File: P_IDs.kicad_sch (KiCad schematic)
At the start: 1 part

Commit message: bored
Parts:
- added U11: ~, symbol PID_symbols:stop
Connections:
- net 1-2: now also U11.
- net TI-HP: now also U11.
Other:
- note added: "[Normally stops are added at the Tee (circle) section]"
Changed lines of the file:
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@@
 	(rectangle
 		(start 62.23 86.36)
-		(end 186.69 121.92)
+		(end 187.325 122.555)
 		(stroke
 			(width 0)
@@
 	)
 	(rectangle
-		(start 154.94 87.63)
+		(start 154.94 88.265)
 		(end 185.42 120.904)
 		(stroke
@@
 	)
 	(rectangle
-		(start 119.38 87.63)
+		(start 119.38 88.265)
 		(end 152.4 120.904)
 		(stroke
@@
 	(text "<-Pipe label\n"
 		(exclude_from_sim no)
-		(at 164.592 99.314 0)
+		(at 164.592 98.679 0)
 		(effects
 			(font
@@
 	(text "stop\nsymbol"
 		(exclude_from_sim no)
-		(at 158.496 111.506 0)
+		(at 161.925 106.68 0)
 		(effects
 			(font
@@
 	(text "<-Pipe label\n"
 		(exclude_from_sim no)
-		(at 178.816 110.744 0)
+		(at 174.625 104.14 0)
 		(effects
 			(font
@@
 	(text "Torch Igniter Pneumatics Line"
 		(exclude_from_sim no)
-		(at 100.33 113.03 0)
+		(at 99.695 113.03 0)
 		(effects
 			(font
@@
 		)
 	)
+	(text "[Normally stops \nare added\nat the Tee \n(circle) section]"
+		(exclude_from_sim no)
+		(at 164.465 114.935 0)
+		(effects
+			(font
+				(size 1.27 1.27)
+				(color 204 102 0 1)
+			)
+		)
+	)
 	(text "->"
 		(exclude_from_sim no)
-		(at 158.75 108.712 90)
+		(at 163.83 103.505 90)
 		(effects
 			(font
@@
 	)
 	(junction
-		(at 157.734 106.68)
+		(at 157.48 101.6)
 		(diameter 0)
 		(color 0 0 0 0)
 	)
-	(wire
-		(pts
-			(xy 159.004 106.68) (xy 171.45 106.68)
-		)
-		(stroke
-			(width 0)
-			(type default)
-		)
+	(junction
+		(at 175.26 114.935)
+		(diameter 0)
+		(color 0 0 0 0)
 	)
 	(wire
@@
 	(wire
 		(pts
-			(xy 157.734 95.25) (xy 157.734 106.68)
+			(xy 175.26 111.125) (xy 175.26 114.935)
+		)
+		(stroke
+			(width 0)
+			(type default)
+		)
+	)
+	(wire
+		(pts
+			(xy 175.26 114.935) (xy 175.26 118.745)
+		)
+		(stroke
+			(width 0)
+			(type default)
+		)
+	)
+	(wire
+		(pts
+			(xy 157.48 94.615) (xy 157.48 101.6)
+		)
+		(stroke
+			(width 0)
+			(type default)
+		)
+	)
+	(wire
+		(pts
+			(xy 157.48 101.6) (xy 163.195 101.6)
 		)
 		(stroke
@@
 	(wire
 		(pts
+			(xy 157.48 101.6) (xy 157.48 106.045)
+		)
+		(stroke
+			(width 0)
+			(type default)
+		)
+	)
+	(wire
+		(pts
 			(xy 66.04 109.22) (xy 74.93 109.22)
 		)
@@
 	(wire
 		(pts
+			(xy 179.705 114.935) (xy 179.705 118.745)
+		)
+		(stroke
+			(width 0)
+			(type default)
+		)
+	)
+	(wire
+		(pts
 			(xy 66.04 93.98) (xy 74.93 93.98)
 		)
@@
 	(wire
 		(pts
-			(xy 157.734 106.68) (xy 157.734 118.11)
+			(xy 164.465 101.6) (xy 168.91 101.6)
 		)
 		(stroke
@@
 	(wire
 		(pts
-			(xy 171.45 106.68) (xy 171.45 111.76)
+			(xy 168.91 101.6) (xy 168.91 106.045)
+		)
+		(stroke
+			(width 0)
+			(type default)
+		)
+	)
+	(wire
+		(pts
+			(xy 176.53 114.935) (xy 179.705 114.935)
 		)
 		(stroke
@@
 		)
 	)
+	(global_label "TI-HP"
+		(shape input)
+		(at 179.705 114.935 270)
+		(fields_autoplaced yes)
+		(effects
+			(font
+				(size 0.254 0.254)
+			)
+			(justify right)
+		)
+		(property "Intersheetrefs" "${INTERSHEET_REFS}"
+			(at 179.705 116.6817 90)
+			(effects
+				(font
+					(size 1.27 1.27)
+				)
+				(justify right)
+				(hide yes)
+			)
+		)
+	)
 	(global_label "3-8"
 		(shape input)
@@
 	(global_label "1-2"
 		(shape input)
-		(at 157.734 99.06 0)
+		(at 157.48 98.425 0)
 		(fields_autoplaced yes)
 		(effects
@@
 		)
 		(property "Intersheetrefs" "${INTERSHEET_REFS}"
-			(at 159.1299 99.06 0)
-			(effects
-				(font
-					(size 1.27 1.27)
-				)
-				(justify left)
+			(at 158.8759 98.425 0)
+			(effects
+				(font
+					(size 1.27 1.27)
+				)
+				(justify left)
+				(hide yes)
+			)
+		)
+	)
+	(global_label "1-2"
+		(shape input)
+		(at 175.26 111.76 270)
+		(fields_autoplaced yes)
+		(effects
+			(font
+				(size 0.254 0.254)
+			)
+			(justify right)
+		)
+		(property "Intersheetrefs" "${INTERSHEET_REFS}"
+			(at 175.26 113.1559 90)
+			(effects
+				(font
+					(size 1.27 1.27)
+				)
+				(justify right)
 				(hide yes)
 			)
@@
 	(global_label "TI-HP"
 		(shape input)
-		(at 171.45 110.49 0)
+		(at 168.91 104.775 90)
 		(fields_autoplaced yes)
 		(effects
@@
 		)
 		(property "Intersheetrefs" "${INTERSHEET_REFS}"
-			(at 173.1967 110.49 0)
+			(at 168.91 103.0283 90)
 			(effects
 				(font
@@
 	(symbol
 		(lib_id "PID_symbols:stop")
-		(at 159.004 106.68 0)
+		(at 164.465 101.6 0)
 		(unit 1)
 		(exclude_from_sim no)
@@
 		(fields_autoplaced yes)
 		(property "Reference" "U6"
-			(at 161.29 106.172 0)
+			(at 166.751 101.092 0)
 			(effects
 				(font
@@
 		)
 		(property "Value" "~"
-			(at 158.369 105.41 0)
+			(at 163.83 100.33 0)
 			(effects
 				(font
@@
 		)
 		(property "Footprint" ""
-			(at 159.004 106.68 0)
+			(at 164.465 101.6 0)
 			(effects
 				(font
@@
 		)
 		(property "Datasheet" ""
-			(at 159.004 106.68 0)
+			(at 164.465 101.6 0)
 			(effects
 				(font
@@
 		)
 		(property "Description" ""
-			(at 159.004 106.68 0)
+			(at 164.465 101.6 0)
 			(effects
 				(font
@@
 					(unit 1)
 				)
+			)
+		)
+	)
+	(symbol
+		(lib_name "stop_1")
+		(lib_id "PID_symbols:stop")
+		(at 176.53 114.935 0)
+		(unit 1)
+		(exclude_from_sim no)
+		(in_bom no)
+		(on_board no)
+		(dnp no)
+		(fields_autoplaced yes)
+		(property "Reference" "U11"
+			(at 178.816 114.427 0)
+			(effects
+				(font
+					(size 1.27 1.27)
+				)
+				(hide yes)
+			)
+		)
+		(property "Value" "~"
+			(at 175.895 113.665 0)
+			(effects
+				(font
+					(size 1.27 1.27)
+				)
+			)
+		)
+		(property "Footprint" ""
+			(at 176.53 114.935 0)
+			(effects
+				(font
+					(size 1.27 1.27)
+				)
+				(hide yes)
+			)
+		)
+		(property "Datasheet" ""
+			(at 176.53 114.935 0)
+			(effects
+				(font
+					(size 1.27 1.27)
+				)
+				(hide yes)
+			)
+		)
+		(property "Description" ""
+			(at 176.53 114.935 0)
+			(effects
+				(font
+					(size 1.27 1.27)
+				)
+				(hide yes)
+			)
+		)
+		(pin ""
+		)
+		(pin ""
+		)
+		(instances
+			(project ""
+				(path "/045f1f05-3134-4b6d-91b6-463031104f1e"
+					(reference "U11")
+					(unit 1)
+				)

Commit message: Baboucarr Jeng
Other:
- added sheet SilwoodDev (SilwoodDev.kicad_sch)

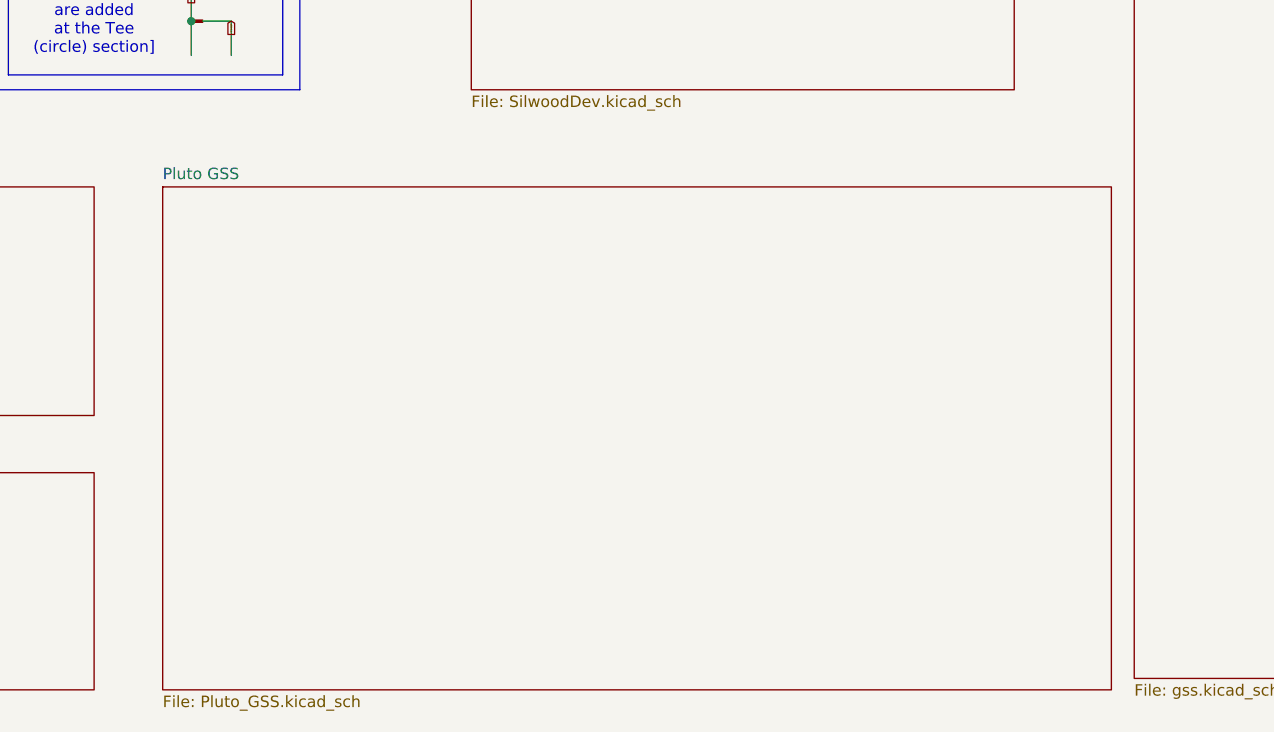
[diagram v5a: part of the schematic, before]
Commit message: Ereg calibration sheet
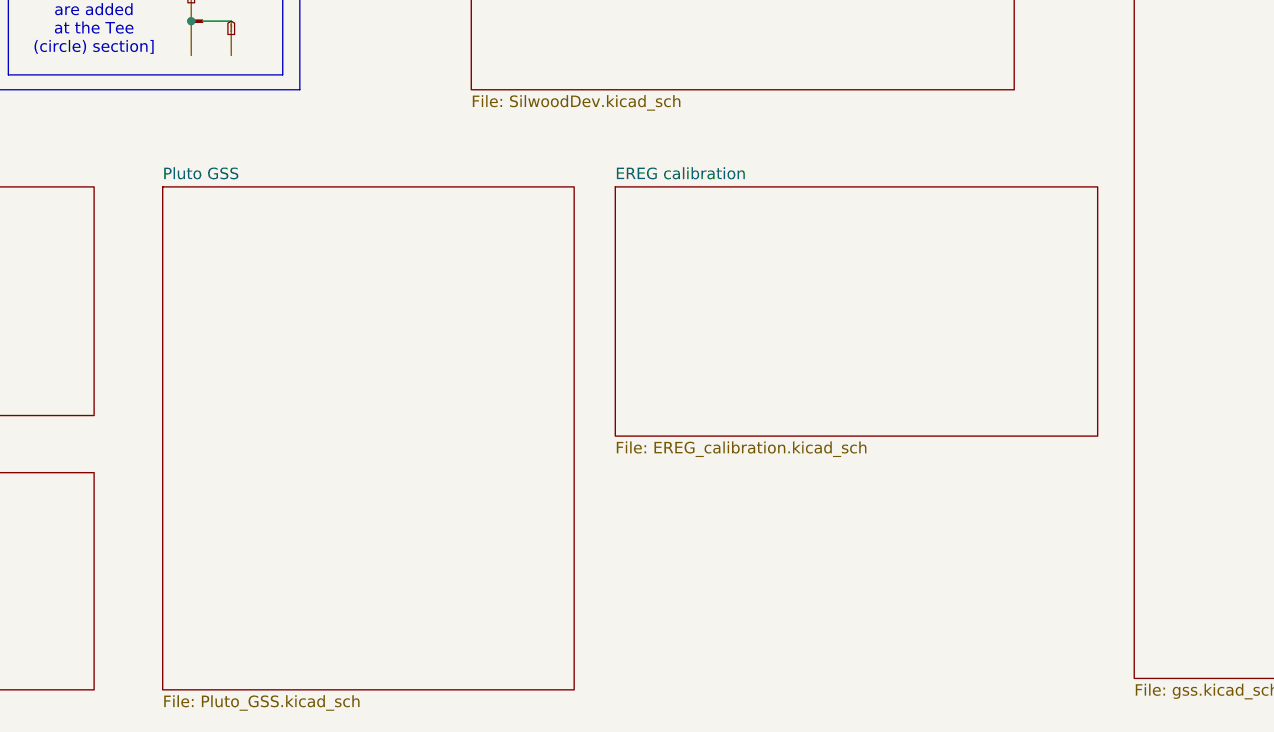
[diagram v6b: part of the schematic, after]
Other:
- added sheet EREG calibration (EREG_calibration.kicad_sch)
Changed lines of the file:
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@@
 	(sheet
 		(at 129.54 134.62)
-		(size 105.41 55.88)
+		(size 45.72 55.88)
 		(exclude_from_sim no)
 		(in_bom yes)
@@
 				)
 			)
+		)
+	)
+	(sheet
+		(at 179.832 134.62)
+		(size 53.594 27.686)
+		(exclude_from_sim no)
+		(in_bom yes)
+		(on_board yes)
+		(dnp no)
+		(fields_autoplaced yes)
+		(stroke
+			(width 0.1524)
+			(type solid)
+		)
+		(fill
+			(color 0 0 0 0.0000)
+		)
+		(property "Sheetname" "EREG calibration"
+			(at 179.832 133.9084 0)
+			(effects
+				(font
+					(size 1.27 1.27)
+				)
+				(justify left bottom)
+			)
+		)
+		(property "Sheetfile" "EREG_calibration.kicad_sch"
+			(at 179.832 162.8906 0)
+			(effects
+				(font
+					(size 1.27 1.27)
+				)
+				(justify left top)
+			)
+		)
+		(instances
+			(project "P_IDs"
+				(path "/045f1f05-3134-4b6d-91b6-463031104f1e"
+					(page "12")
+				)
+			)
